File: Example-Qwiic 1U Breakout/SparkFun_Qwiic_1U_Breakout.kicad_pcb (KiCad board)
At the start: 2 copper layers, 25.4 x 25.4 mm, 67 parts, among them J1 Qwiic_RA, J2 Qwiic_RA, J3 Conn_01x06, Q1 BSS138, Q2 BSS138, U5 AP3012

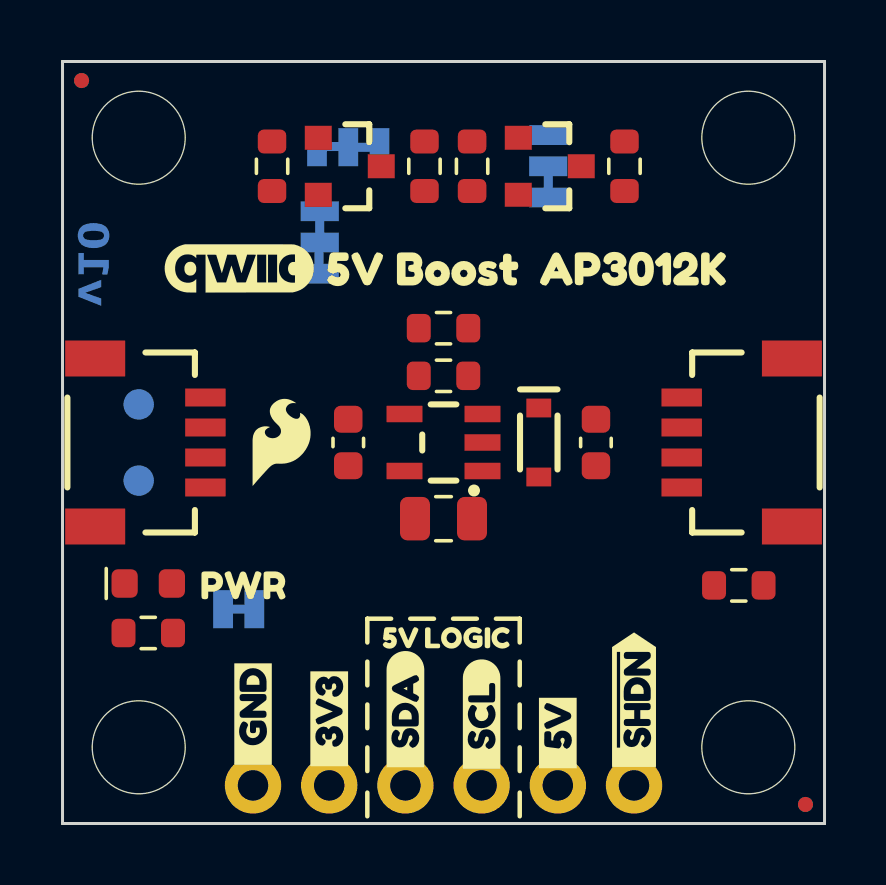
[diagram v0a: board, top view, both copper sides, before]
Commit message: Modify copper to edge constraint
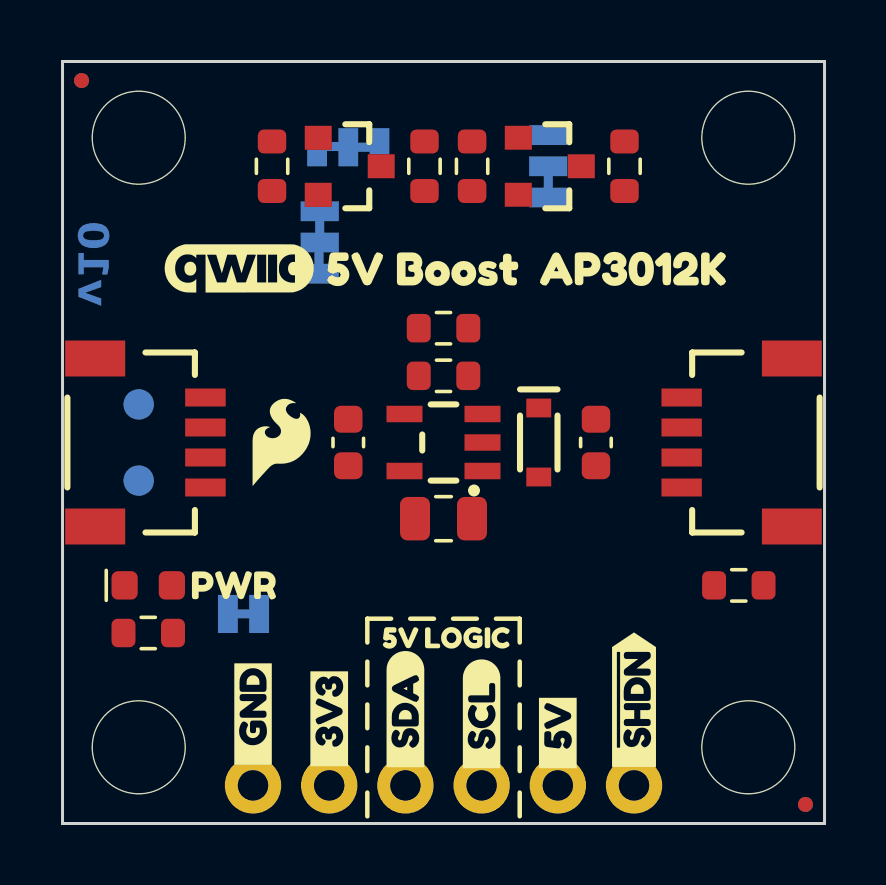
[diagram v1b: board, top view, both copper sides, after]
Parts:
- removed kibuzzard-67D9D9D8: G***, kibuzzard-67D9D9D8
- added kibuzzard-67D9E7C1: G***, kibuzzard-67D9E7C1, B.Cu at (126.4, 103.8)
- moved kibuzzard-65A8A8B4 0.32 mm to (129.0, 102.9)
- moved JP1 0.22 mm to (129.3, 103.8)
- moved D1 0.06 mm to (126.1, 102.9)

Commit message: Rename Basic Board folder
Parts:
- J1, J2: footprint SparkFun-Connector:JST_SMD_1.0mm-4_RA -> SparkFun-Connector:JST_SMD_1.0mm-4_Black
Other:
- board text added: "Finish: HASL Lead-Free"
- board text removed: "Finish: Lead-Free HASL"

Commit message: Make labels fit standard
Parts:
- removed kibuzzard-65A8A8B4: G***, kibuzzard-65A8A8B4
- removed kibuzzard-67A51507 (x2): G***, kibuzzard-67A51507
- removed kibuzzard-67A51B2D: G***, kibuzzard-67A51B2D
- removed kibuzzard-67A51CFE (x2): G***, kibuzzard-67A51CFE
- removed kibuzzard-67AB7F1B: G***, kibuzzard-67AB7F1B
- removed kibuzzard-67AB7F2D: G***, kibuzzard-67AB7F2D
- removed kibuzzard-67BF5EEE (x2): G***, kibuzzard-67BF5EEE
- removed kibuzzard-67BF5EF7 (x2): G***, kibuzzard-67BF5EF7
- removed kibuzzard-67BF7C99: G***, kibuzzard-67BF7C99
- removed kibuzzard-67BF7CAB: G***, kibuzzard-67BF7CAB
- removed kibuzzard-67BF7CFE: G***, kibuzzard-67BF7CFE
- removed kibuzzard-67BF7D12: G***, kibuzzard-67BF7D12
- removed kibuzzard-67BF7D5E: G***, kibuzzard-67BF7D5E
- removed kibuzzard-67BF7D85: G***, kibuzzard-67BF7D85
- removed kibuzzard-67BF7EBF: G***, kibuzzard-67BF7EBF
- removed kibuzzard-67BF7ED9: G***, kibuzzard-67BF7ED9
- removed kibuzzard-67BF7F13: G***, kibuzzard-67BF7F13
- removed kibuzzard-67BF7F2F: G***, kibuzzard-67BF7F2F
- removed kibuzzard-67BF7F4D: G***, kibuzzard-67BF7F4D
- removed kibuzzard-67BF7F7D: G***, kibuzzard-67BF7F7D
- removed kibuzzard-67D9D97F: G***, kibuzzard-67D9D97F
- removed kibuzzard-67D9D996: G***, kibuzzard-67D9D996
- removed kibuzzard-67D9D9A8: G***, kibuzzard-67D9D9A8
- removed kibuzzard-67D9D9B3: G***, kibuzzard-67D9D9B3
- removed kibuzzard-67D9E7C1: G***, kibuzzard-67D9E7C1
- added kibuzzard-689A5B87: G***, kibuzzard-689A5B87, B.Cu at (142.0, 87.9)
- added kibuzzard-689A5B91: G***, kibuzzard-689A5B91, B.Cu at (141.7, 89.9)
- added kibuzzard-689A5B9F: G***, kibuzzard-689A5B9F, B.Cu at (126.4, 103.8)
- added kibuzzard-689A5BBE: G***, kibuzzard-689A5BBE, F.Cu at (132.2, 107.3)
- added kibuzzard-689A5BCF: G***, kibuzzard-689A5BCF, F.Cu at (134.7, 107.0)
- added kibuzzard-689A5BE6: G***, kibuzzard-689A5BE6, F.Cu at (139.8, 107.8)
- added kibuzzard-689A5BFD: G***, kibuzzard-689A5BFD, B.Cu at (128.3, 91.4)
- added kibuzzard-689A5C01: G***, kibuzzard-689A5C01, B.Cu at (129.6, 88.3)
- added kibuzzard-689A5C0D: G***, kibuzzard-689A5C0D, B.Cu at (129.6, 107.2)
- added kibuzzard-689A5C20: G***, kibuzzard-689A5C20, B.Cu at (134.7, 107.0)
- added kibuzzard-689A5C2B: G***, kibuzzard-689A5C2B, B.Cu at (139.8, 107.8)
- added kibuzzard-689A5E8C: G***, kibuzzard-689A5E8C, B.Cu at (142.3, 106.7)
- added kibuzzard-689A5E95: G***, kibuzzard-689A5E95, F.Cu at (142.3, 106.7)
- added kibuzzard-689A5ED7: G***, kibuzzard-689A5ED7, F.Cu at (137.2, 107.2)
- added kibuzzard-689A5EDF: G***, kibuzzard-689A5EDF, B.Cu at (137.2, 107.2)
- added kibuzzard-689A5EF4: G***, kibuzzard-689A5EF4, F.Cu at (129.6, 107.2)
- added kibuzzard-689A5EFF: G***, kibuzzard-689A5EFF, B.Cu at (132.2, 107.3)
- added kibuzzard-689A6411: G***, kibuzzard-689A6411, F.Cu at (142.3, 92.4)
- added kibuzzard-689A6418: G***, kibuzzard-689A6418, F.Cu at (135.3, 92.4)
- added kibuzzard-689A642E: G***, kibuzzard-689A642E, F.Cu at (129.1, 102.9)
- added kibuzzard-689A644B: G***, kibuzzard-689A644B, B.Cu at (136.0, 88.9)
- added kibuzzard-689A6454: G***, kibuzzard-689A6454, B.Cu at (136.9, 88.9)
- added kibuzzard-689A6468: G***, kibuzzard-689A6468, B.Cu at (137.9, 88.9)
- added kibuzzard-689A6479: G***, kibuzzard-689A6479, B.Cu at (136.0, 100.3)
- added kibuzzard-689A6481: G***, kibuzzard-689A6481, B.Cu at (136.0, 102.2)
- added kibuzzard-689A648B: G***, kibuzzard-689A648B, B.Cu at (135.3, 104.6)
- added kibuzzard-689A6494: G***, kibuzzard-689A6494, B.Cu at (137.6, 104.6)
- added kibuzzard-689A649F: G***, kibuzzard-689A649F, F.Cu at (136.8, 104.6)
- added kibuzzard-689A64A8: G***, kibuzzard-689A64A8, F.Cu at (134.5, 104.6)
- moved G*** 0.16 mm to (136.0, 95.9)
- moved G*** 0.16 mm to (136.0, 98.1)
- moved G*** 0.10 mm to (129.2, 92.4)

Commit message: Make labels and text follow standard
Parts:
- removed kibuzzard-689A5B87: G***, kibuzzard-689A5B87
- removed kibuzzard-689A5B91: G***, kibuzzard-689A5B91
- removed kibuzzard-689A5B9F: G***, kibuzzard-689A5B9F
- removed kibuzzard-689A5BBE: G***, kibuzzard-689A5BBE
- removed kibuzzard-689A5BCF: G***, kibuzzard-689A5BCF
- removed kibuzzard-689A5BE6: G***, kibuzzard-689A5BE6
- removed kibuzzard-689A5BFD: G***, kibuzzard-689A5BFD
- removed kibuzzard-689A5C01: G***, kibuzzard-689A5C01
- removed kibuzzard-689A5C0D: G***, kibuzzard-689A5C0D
- removed kibuzzard-689A5C20: G***, kibuzzard-689A5C20
- removed kibuzzard-689A5C2B: G***, kibuzzard-689A5C2B
- removed kibuzzard-689A5E8C: G***, kibuzzard-689A5E8C
- removed kibuzzard-689A5E95: G***, kibuzzard-689A5E95
- removed kibuzzard-689A5ED7: G***, kibuzzard-689A5ED7
- removed kibuzzard-689A5EDF: G***, kibuzzard-689A5EDF
- removed kibuzzard-689A5EF4: G***, kibuzzard-689A5EF4
- removed kibuzzard-689A5EFF: G***, kibuzzard-689A5EFF
- removed kibuzzard-689A6468: G***, kibuzzard-689A6468
- added kibuzzard-689A66E2: G***, kibuzzard-689A66E2, F.Cu at (129.6, 107.2)
- added kibuzzard-689A66E9: G***, kibuzzard-689A66E9, F.Cu at (132.2, 107.3)
- added kibuzzard-689A66EE: G***, kibuzzard-689A66EE, F.Cu at (134.7, 107.0)
- added kibuzzard-689A66F4: G***, kibuzzard-689A66F4, F.Cu at (137.2, 107.2)
- added kibuzzard-689A66F9: G***, kibuzzard-689A66F9, F.Cu at (139.8, 107.8)
- added kibuzzard-689A66FE: G***, kibuzzard-689A66FE, F.Cu at (142.3, 106.7)
- added kibuzzard-689A6706: G***, kibuzzard-689A6706, B.Cu at (142.3, 106.7)
- added kibuzzard-689A670C: G***, kibuzzard-689A670C, B.Cu at (139.8, 107.8)
- added kibuzzard-689A6711: G***, kibuzzard-689A6711, B.Cu at (137.2, 107.2)
- added kibuzzard-689A6718: G***, kibuzzard-689A6718, B.Cu at (134.7, 107.0)
- added kibuzzard-689A6721: G***, kibuzzard-689A6721, B.Cu at (132.2, 107.3)
- added kibuzzard-689A6728: G***, kibuzzard-689A6728, B.Cu at (129.6, 107.2)
- added kibuzzard-689A6759: G***, kibuzzard-689A6759, B.Cu at (129.6, 88.3)
- added kibuzzard-689A6762: G***, kibuzzard-689A6762, B.Cu at (128.3, 91.4)
- added kibuzzard-689A676B: G***, kibuzzard-689A676B, B.Cu at (141.7, 89.9)
- added kibuzzard-689A6771: G***, kibuzzard-689A6771, B.Cu at (142.0, 87.9)
- added kibuzzard-689A6775: G***, kibuzzard-689A6775, B.Cu at (137.9, 88.9)
- added kibuzzard-689A6796: G***, kibuzzard-689A6796, B.Cu at (126.4, 103.8)

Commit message: Update examples with latest parts
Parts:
- J1, J2: footprint SparkFun-Connector:JST_SMD_1.0mm-4_Black -> SparkFun-Connector:JST_1x04_P1.0mm_Horizontal_SMD
- J3: footprint SparkFun-Connector:1x06 -> SparkFun-Connector:1x06_P2.54mm
